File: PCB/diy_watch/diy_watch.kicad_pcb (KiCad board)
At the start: 2 copper layers, 35.9 x 36.9 mm, 44 parts, among them IC1 W25Q16JVUXIQ, J1 USB_B_Micro, SW1 SW_Push, U2 DS3231MZ, U3 RP2040, U7 XC6210B332MR, U8 LTC4071EMS8E_PBF, Y1 12MHz_crystal

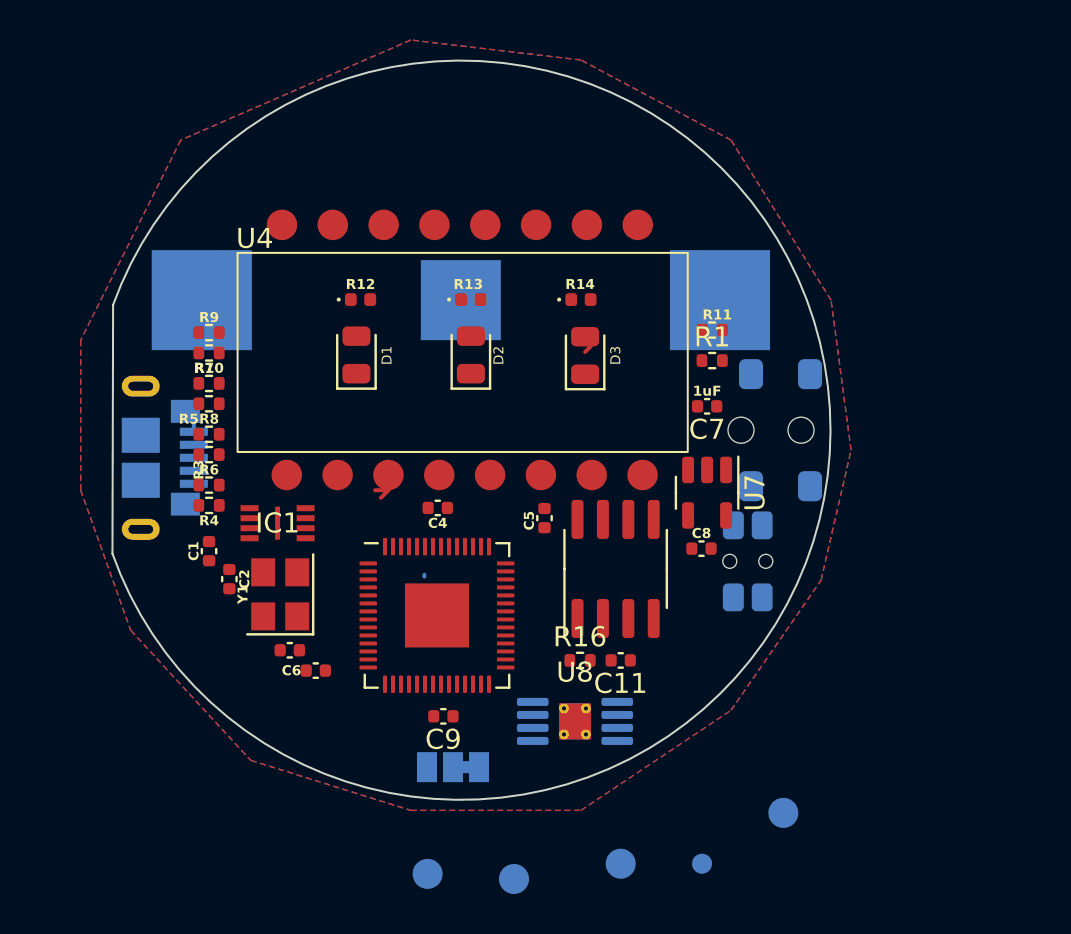
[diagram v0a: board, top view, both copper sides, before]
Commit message: Re-routed refactored board
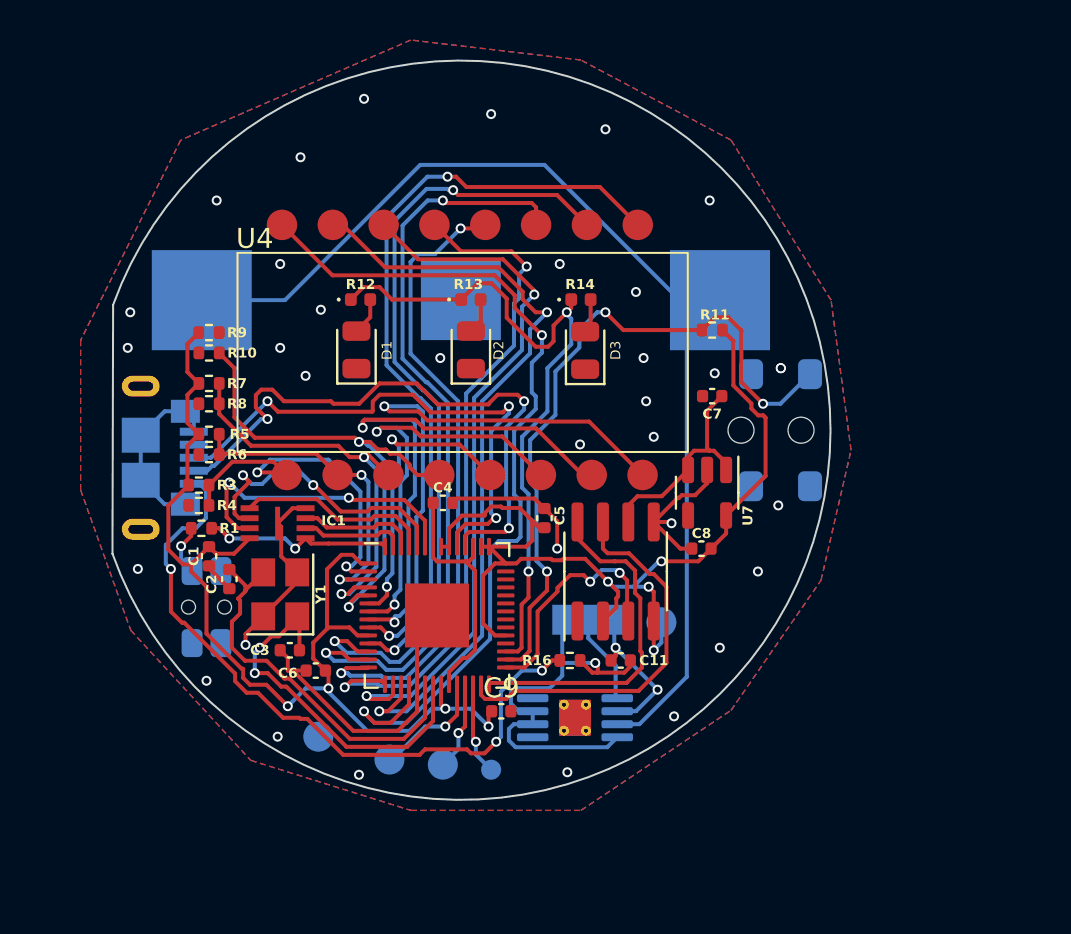
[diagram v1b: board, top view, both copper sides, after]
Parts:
- moved SW1 27.1 mm to (137.3, 108.8), turned to 90 degrees
- moved R1 26.9 mm to (137.0, 104.9)
- moved TP2 16.4 mm to (142.9, 115.3)
- moved TP4 11.5 mm to (151.5, 117.0)
- moved TP5 11.3 mm to (160.0, 109.6)
- moved JP1 10.00 mm to (156.4, 109.5)
- moved TP3 6.73 mm to (149.1, 116.7)
- moved TP1 6.02 mm to (146.4, 116.5)
- moved C9 2.90 mm to (152.0, 114.0), turned to 0 degrees
- moved C7 0.57 mm to (162.6, 98.3)
- moved R4 0.51 mm to (136.9, 103.8)
- moved R16 0.51 mm to (155.4, 111.5)
- moved R3 0.51 mm to (136.9, 102.7)
- moved C4 0.36 mm to (149.1, 103.6), turned to 0 degrees
- moved C1 0.25 mm to (137.4, 106.3)
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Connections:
- BT1 pad 1: Net-(BT1-+) -> +BATT
- R16 pad 1: +BATT -> +5V
- U8 pad 7: Net-(BT1-+) -> +BATT
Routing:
- net +3.3V: track 0.00 -> 103.1 mm, vias 0 -> 8
- net +BATT: track 0.00 -> 67.1 mm
- net GND: track 1.19 -> 57.4 mm, vias 0 -> 36
- net /L: track 0.00 -> 45.1 mm, vias 0 -> 2
- net /F: track 0.00 -> 40.4 mm, vias 0 -> 2
- net /E: track 0.00 -> 39.2 mm, vias 0 -> 2
- net /K: track 0.00 -> 39.0 mm, vias 0 -> 2
- net /G: track 0.00 -> 38.8 mm, vias 0 -> 2
- net /J: track 0.00 -> 35.9 mm, vias 0 -> 2
- net /light_sw: track 0.11 -> 35.7 mm, vias 0 -> 3
- net /light_en: track 0.00 -> 34.4 mm, vias 0 -> 2
- net /I: track 0.00 -> 34.4 mm, vias 0 -> 2
- net +5V: track 0.00 -> 34.2 mm, vias 0 -> 3
- net /H: track 0.00 -> 32.2 mm, vias 0 -> 2
- net /usb_D-: track 0.00 -> 30.9 mm, vias 0 -> 3
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
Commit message: Fixing DRC errors on PCB
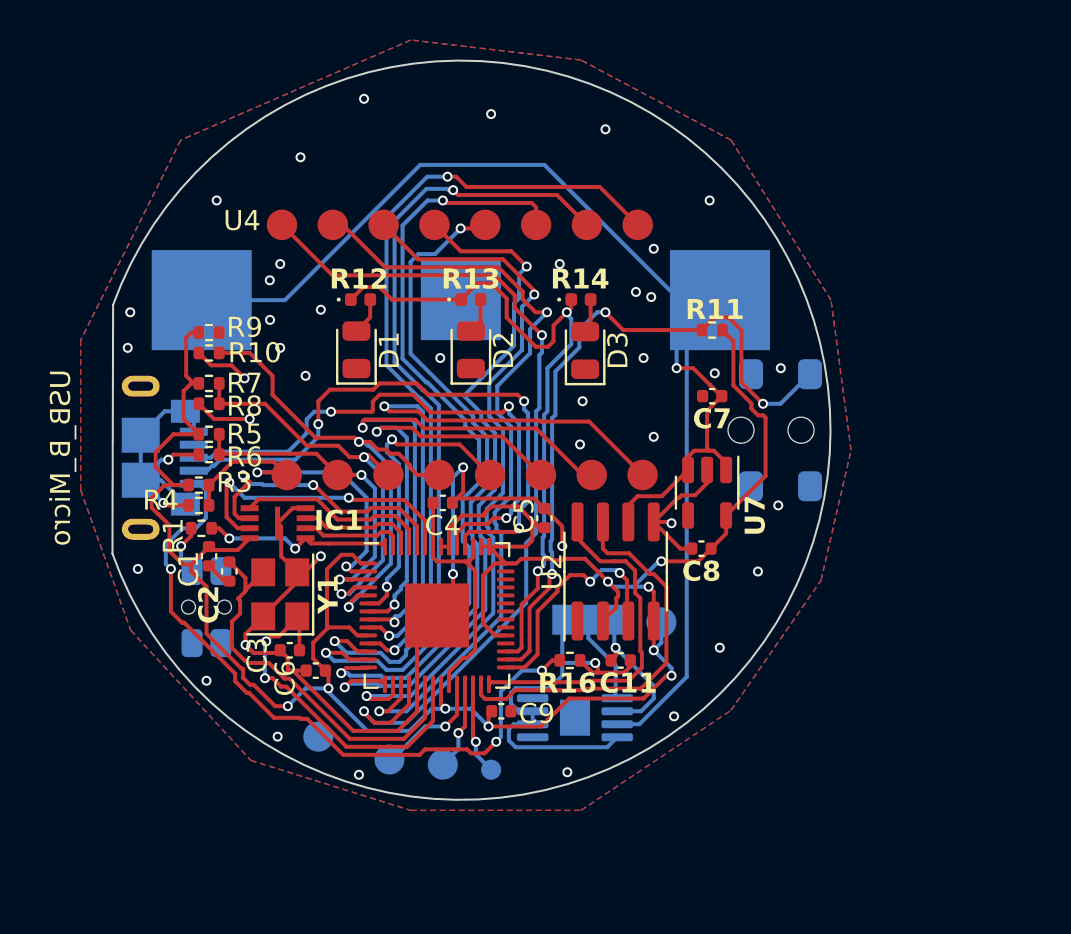
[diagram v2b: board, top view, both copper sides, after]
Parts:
- U8: footprint Package_SO:MSOP-8-1EP_3x3mm_P0.65mm_EP1.5x1.8mm_ThermalVias -> Package_SO:MSOP-8-1EP_3x3mm_P0.65mm_EP1.5x1.8mm
- moved C2 0.38 mm to (138.4, 107.1)
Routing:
- net GND: track 57.4 -> 82.8 mm, vias 36 -> 45
- net +3.3V: track 103.1 -> 119.5 mm, vias 8 -> 9
- net +BATT: track 67.1 -> 74.2 mm, vias 0 -> 1
- net /G: track 38.8 -> 40.3 mm
- net /I: track 34.4 -> 36.0 mm
- net /H: track 32.2 -> 33.6 mm
- net /usb_D-: track 30.9 -> 29.7 mm
- net /L: track 45.1 -> 44.1 mm
- net /K: track 39.0 -> 39.8 mm
- net /J: track 35.9 -> 36.7 mm
- net /light_sw: track 35.7 -> 35.1 mm
- net /COM4: track 26.0 -> 25.4 mm
- net Net-(IC1-CLK): track 14.7 -> 14.1 mm
- net Net-(U3-XOUT): track 18.5 -> 17.9 mm
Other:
- rule pad_to_mask_clearance: 0 -> 0.038

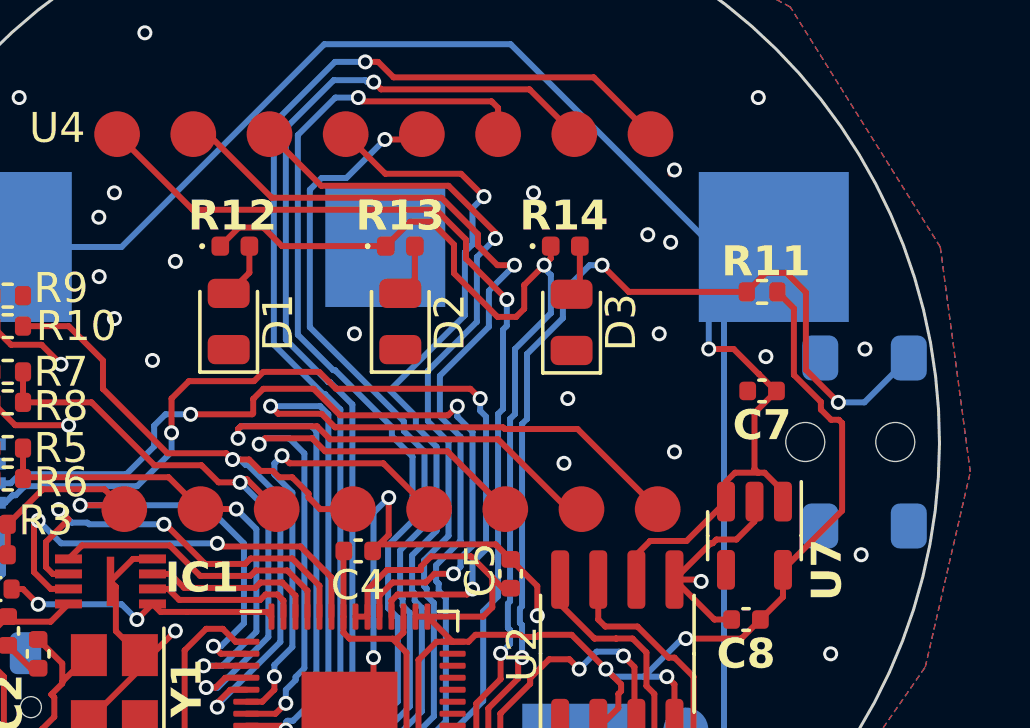
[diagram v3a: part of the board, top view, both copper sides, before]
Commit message: Updating components for stock reasons
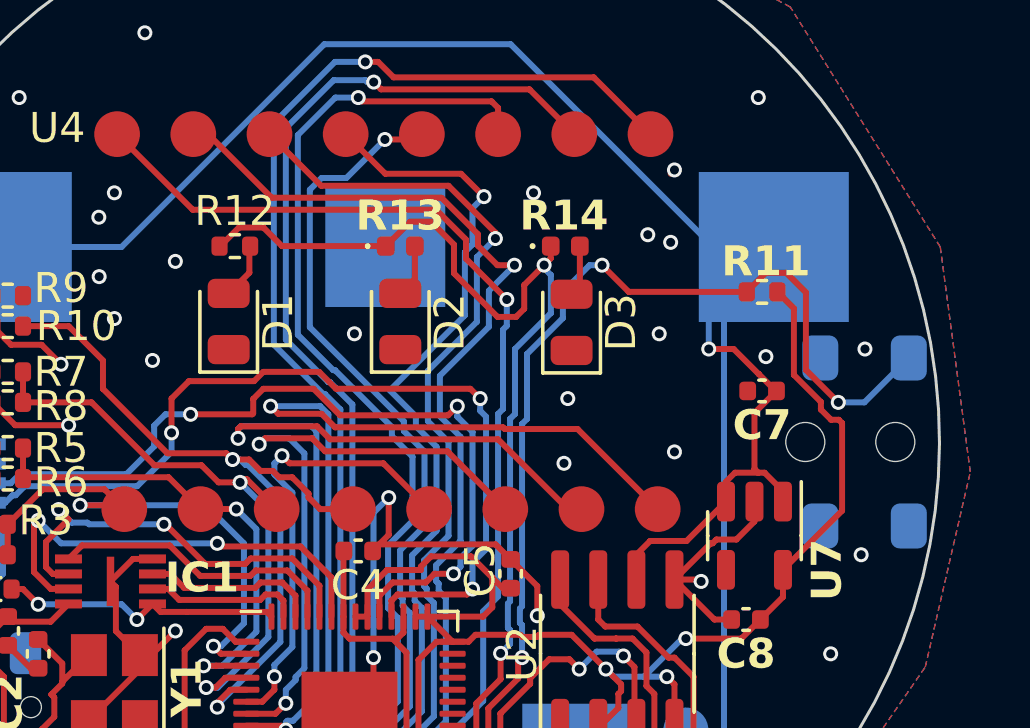
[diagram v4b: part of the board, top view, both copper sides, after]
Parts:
- removed U6: ~, DIY_Watch_lib:Diptronics FTE-3
- added U1: FTE-2CA-V-T/R, DIY_Watch_lib:Diptronics FTE-3, B.Cu at (164.5, 100.0)
- R12: footprint LED_SMD:LED_0402_1005Metric -> Resistor_SMD:R_0402_1005Metric
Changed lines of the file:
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@@
   (net 47 "/RTC_SCL")
   (net 48 "/light_sw")
-  (net 49 "unconnected-(U6-Pad2)")
-  (net 50 "unconnected-(U6-Pad4)")
+  (net 49 "unconnected-(U1-Pad2)")
+  (net 50 "unconnected-(U1-Pad4)")
   (net 51 "unconnected-(U8-NTCBIAS-Pad1)")
   (net 52 "unconnected-(U8-HBO-Pad4)")
@@
     )
   )
-  (footprint "LED_SMD:LED_0402_1005Metric" (layer "F.Cu")
+  (footprint "Resistor_SMD:R_0402_1005Metric" (layer "F.Cu")
     (at 144.985 93.472)
-    (descr "LED SMD 0402 (1005 Metric), square (rectangular) end terminal, IPC_7351 nominal, (Body size source: http://www.tortai-tech.com/upload/download/2011102023233369053.pdf), generated with kicad-footprint-generator")
-    (tags "LED")
+    (descr "Resistor SMD 0402 (1005 Metric), square (rectangular) end terminal, IPC_7351 nominal, (Body size source: IPC-SM-782 page 72, https://www.pcb-3d.com/wordpress/wp-content/uploads/ipc-sm-782a_amendment_1_and_2.pdf), generated with kicad-footprint-generator")
+    (tags "resistor")
     (property "Sheetfile" "diy_watch.kicad_sch")
     (property "Sheetname" "")
@@
     (property "ki_keywords" "R res resistor")
     (attr smd)
-    (fp_text reference "R12" (at -0.078 -1.016) (layer "F.SilkS")
-        (effects (font (size 1 1) (thickness 0.153) bold))
+    (fp_text reference "R12" (at 0 -1.17) (layer "F.SilkS")
+        (effects (font (size 1 1) (thickness 0.15)))
     )
-    (fp_text value "300" (at 0 1.17) (layer "F.SilkS") hide
-        (effects (font (size 1 1) (thickness 0.153)))
+    (fp_text value "300" (at 0 1.17) (layer "F.Fab")
+        (effects (font (size 1 1) (thickness 0.15)))
     )
     (fp_text user "${REFERENCE}" (at 0 0) (layer "F.Fab")
-        (effects (font (size 0.25 0.25) (thickness 0.04)))
+        (effects (font (size 0.26 0.26) (thickness 0.04)))
     )
-    (fp_circle (center -1.09 0) (end -1.04 0)
-      (stroke (width 0.1) (type solid)) (fill none) (layer "F.SilkS"))
+    (fp_line (start -0.153641 -0.38) (end 0.153641 -0.38)
+      (stroke (width 0.12) (type solid)) (layer "F.SilkS"))
+    (fp_line (start -0.153641 0.38) (end 0.153641 0.38)
+      (stroke (width 0.12) (type solid)) (layer "F.SilkS"))
     (fp_line (start -0.93 -0.47) (end 0.93 -0.47)
       (stroke (width 0.05) (type solid)) (layer "F.CrtYd"))
@@
     (fp_line (start 0.93 0.47) (end -0.93 0.47)
       (stroke (width 0.05) (type solid)) (layer "F.CrtYd"))
-    (fp_line (start -0.5 -0.25) (end 0.5 -0.25)
-      (stroke (width 0.1) (type solid)) (layer "F.Fab"))
-    (fp_line (start -0.5 0.25) (end -0.5 -0.25)
-      (stroke (width 0.1) (type solid)) (layer "F.Fab"))
-    (fp_line (start -0.4 0.25) (end -0.4 -0.25)
+    (fp_line (start -0.525 -0.27) (end 0.525 -0.27)
       (stroke (width 0.1) (type solid)) (layer "F.Fab"))
-    (fp_line (start -0.3 0.25) (end -0.3 -0.25)
+    (fp_line (start -0.525 0.27) (end -0.525 -0.27)
       (stroke (width 0.1) (type solid)) (layer "F.Fab"))
-    (fp_line (start 0.5 -0.25) (end 0.5 0.25)
+    (fp_line (start 0.525 -0.27) (end 0.525 0.27)
       (stroke (width 0.1) (type solid)) (layer "F.Fab"))
-    (fp_line (start 0.5 0.25) (end -0.5 0.25)
+    (fp_line (start 0.525 0.27) (end -0.525 0.27)
       (stroke (width 0.1) (type solid)) (layer "F.Fab"))
-    (pad "1" smd roundrect (at -0.485 0) (size 0.59 0.64) (layers "F.Cu" "F.Paste" "F.Mask") (roundrect_rratio 0.25)
+    (pad "1" smd roundrect (at -0.51 0) (size 0.54 0.64) (layers "F.Cu" "F.Paste" "F.Mask") (roundrect_rratio 0.25)
       (net 46 "/light_en") (pintype "passive"))
-    (pad "2" smd roundrect (at 0.485 0) (size 0.59 0.64) (layers "F.Cu" "F.Paste" "F.Mask") (roundrect_rratio 0.25)
+    (pad "2" smd roundrect (at 0.51 0) (size 0.54 0.64) (layers "F.Cu" "F.Paste" "F.Mask") (roundrect_rratio 0.25)
       (net 31 "Net-(D1-A)") (pintype "passive"))
-    (model "${KICAD6_3DMODEL_DIR}/LED_SMD.3dshapes/LED_0402_1005Metric.wrl"
+    (model "${KICAD6_3DMODEL_DIR}/Resistor_SMD.3dshapes/R_0402_1005Metric.wrl"
       (offset (xyz 0 0 0))
       (scale (xyz 1 1 1))
@@
     )
   )
-  (footprint "DIY_Watch_lib:Diptronics FTE-3" (layer "B.Cu")
-    (at 164.5 100 180)
-    (property "Sheetfile" "diy_watch.kicad_sch")
-    (property "Sheetname" "")
-    (attr smd)
-    (fp_text reference "U6" (at -1.108 -1.346 unlocked) (layer "B.SilkS")
-        (effects (font (size 1 1) (thickness 0.153)))
-    )
-    (fp_text value "~" (at 0.25 -13.5 unlocked) (layer "F.SilkS") hide
-        (effects (font (size 1 1) (thickness 0.153)) (justify mirror))
-    )
-    (fp_rect (start -5.65 0.6) (end -3.75 -0.6)
-      (stroke (width 0.1) (type default)) (fill none) (layer "B.Fab"))
-    (fp_rect (start 1.8 2) (end -3.75 -2)
-      (stroke (width 0.1) (type default)) (fill none) (layer "B.Fab"))
-    (fp_circle (center -5.65 0) (end -5.05 0)
-      (stroke (width 0.1) (type default)) (fill none) (layer "B.Fab"))
-    (pad "" np_thru_hole circle (at -2.5 0 90) (size 0.9 0.9) (drill 1.3) (layers "F&B.Cu" "*.Mask"))
-    (pad "" np_thru_hole circle (at 0.5 0 90) (size 0.9 0.9) (drill 1.3) (layers "F&B.Cu" "*.Mask"))
-    (pad "1" smd roundrect (at -2.95 2.8 90) (size 1.5 1.2) (layers "B.Cu" "B.Paste" "B.Mask") (roundrect_rratio 0.25)
-      (net 48 "/light_sw") (pintype "passive") (thermal_bridge_angle 45))
-    (pad "2" smd roundrect (at 0 2.8 90) (size 1.5 1.2) (layers "B.Cu" "B.Paste" "B.Mask") (roundrect_rratio 0.25)
-      (net 49 "unconnected-(U6-Pad2)") (pintype "passive+no_connect") (thermal_bridge_angle 45))
-    (pad "3" smd roundrect (at -2.95 -2.8 90) (size 1.5 1.2) (layers "B.Cu" "B.Paste" "B.Mask") (roundrect_rratio 0.25)
-      (net 2 "GND") (pintype "passive") (thermal_bridge_angle 45))
-    (pad "4" smd roundrect (at 0 -2.8 90) (size 1.5 1.2) (layers "B.Cu" "B.Paste" "B.Mask") (roundrect_rratio 0.25)
-      (net 50 "unconnected-(U6-Pad4)") (pintype "passive+no_connect") (thermal_bridge_angle 45))
-  )
   (footprint "TestPoint:TestPoint_Pad_D1.5mm" (layer "B.Cu")
     (at 142.875 115.316 180)
@@
     )
   )
+  (footprint "DIY_Watch_lib:Diptronics FTE-3" (layer "B.Cu")
+    (at 164.5006 99.9998 180)
+    (property "Sheetfile" "diy_watch.kicad_sch")
+    (property "Sheetname" "")
+    (attr smd)
+    (fp_text reference "U1" (at 0.25 -10 unlocked) (layer "B.SilkS")
+        (effects (font (size 1 1) (thickness 0.1)) (justify mirror))
+    )
+    (fp_text value "FTE-2CA-V-T/R" (at 0.25 -13.5 unlocked) (layer "B.Fab")
+        (effects (font (size 1 1) (thickness 0.15)) (justify mirror))
+    )
+    (fp_text user "${REFERENCE}" (at -0.5 -11.5 unlocked) (layer "B.Fab")
+        (effects (font (size 1 1) (thickness 0.15)) (justify mirror))
+    )
+    (fp_rect (start -5.65 0.6) (end -3.75 -0.6)
+      (stroke (width 0.1) (type default)) (fill none) (layer "B.SilkS"))
+    (fp_rect (start 1.8 2) (end -3.75 -2)
+      (stroke (width 0.1) (type default)) (fill none) (layer "B.SilkS"))
+    (fp_circle (center -5.65 0) (end -5.65 0.6)
+      (stroke (width 0.1) (type default)) (fill none) (layer "B.SilkS"))
+    (pad "" np_thru_hole circle (at -2.5 0 90) (size 1.3 1.3) (drill 1.3) (layers "F&B.Cu" "*.Mask"))
+    (pad "" np_thru_hole circle (at 0.5 0 90) (size 1.3 1.3) (drill 1.3) (layers "F&B.Cu" "*.Mask"))
+    (pad "1" smd roundrect (at -2.95 2.8 90) (size 1.5 1.2) (layers "B.Cu" "B.Paste" "B.Mask") (roundrect_rratio 0.25)
+      (net 48 "/light_sw") (pintype "passive") (thermal_bridge_angle 45))
+    (pad "2" smd roundrect (at 0 2.8 90) (size 1.5 1.2) (layers "B.Cu" "B.Paste" "B.Mask") (roundrect_rratio 0.25)
+      (net 49 "unconnected-(U1-Pad2)") (pintype "passive+no_connect") (thermal_bridge_angle 45))
+    (pad "3" smd roundrect (at -2.95 -2.8 90) (size 1.5 1.2) (layers "B.Cu" "B.Paste" "B.Mask") (roundrect_rratio 0.25)
+      (net 2 "GND") (pintype "passive") (thermal_bridge_angle 45))
+    (pad "4" smd roundrect (at 0 -2.8 90) (size 1.5 1.2) (layers "B.Cu" "B.Paste" "B.Mask") (roundrect_rratio 0.25)
+      (net 50 "unconnected-(U1-Pad4)") (pintype "passive+no_connect") (thermal_bridge_angle 45))
+  )
   (gr_arc (start 132.620296 93.737637) (mid 168.473467 100.04798) (end 132.588 106.172)
